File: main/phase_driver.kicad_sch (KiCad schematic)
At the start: 12 parts, among them Q201 TK4R3E06PL, Q202 TK4R3E06PL, U201 LM2105

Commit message: Start route PCB
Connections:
- net INH: now also U201.2 (INH); no longer U201. (VDD)
- net INL: now also U201.3 (INL); no longer U201. (VDD)
- net OUT: now also U201.6 (SH); no longer U201. (VDD)
- net V_{DRIVE}: now also U201.1 (VDD); no longer U201. (VDD)
- net at C202.1: now also U201.8 (BST); no longer U201. (VDD)
- net at Q202.1 (G): now also U201.5 (GL); no longer U201. (VDD)
- net at Q201.1 (G): now also U201.7 (GH); no longer U201. (VDD)
- net PGND renamed GND
- net GND: now also U201.4 (GND), U201.9 (GND); no longer U201. (VDD)
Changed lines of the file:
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@@
 			)
 		)
-		(pin ""
+		(pin "3"
 		)
-		(pin ""
+		(pin "9"
 		)
-		(pin ""
+		(pin "6"
 		)
-		(pin ""
+		(pin "1"
 		)
-		(pin ""
+		(pin "4"
 		)
-		(pin ""
+		(pin "7"
 		)
-		(pin ""
+		(pin "2"
 		)
-		(pin ""
+		(pin "5"
+		)
+		(pin "8"
 		)
 		(instances

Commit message: Route of power rails
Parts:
- removed C201, C204: 1n, Capacitor_SMD:C_0805_2012Metric, symbol Device:C

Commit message: Clean silkscreen
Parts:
- renumbered C202 to C1001, C203 to C1002, C205 to C1003, D201 to D1001, D202 to D1002, Q201 to Q1001, Q202 to Q1002, R201 to R1001, R202 to R1002, U201 to U1001

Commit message: Sent to fab
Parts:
- C1001: MPN (none) -> CL21B104KACNFNC; Mouser SKU (none) -> 187-CL21B104KACNFNC
- C1003: MPN (none) -> CL21B105KLFVPNE; Mouser SKU (none) -> 187-CL21B105KLFVPNE
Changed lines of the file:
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@@
+			)
+		)
+		(property "Quantity" ""
+			(at 190.5 57.15 0)
+			(effects
+				(font
+					(size 1.27 1.27)
+				)
 			)
 		)
@@
 			)
 		)
+		(property "MPN" "CL21B104KACNFNC "
+			(at 140.97 58.42 0)
+			(effects
+				(font
+					(size 1.27 1.27)
+				)
+			)
+		)
+		(property "Mouser SKU" " 187-CL21B104KACNFNC "
+			(at 140.97 58.42 0)
+			(effects
+				(font
+					(size 1.27 1.27)
+				)
+			)
+		)
+		(property "Quantity" ""
+			(at 140.97 58.42 0)
+			(effects
+				(font
+					(size 1.27 1.27)
+				)
+			)
+		)
 		(pin "1"
 		)
@@
 			)
 		)
+		(property "Quantity" ""
+			(at 228.6 68.58 0)
+			(effects
+				(font
+					(size 1.27 1.27)
+				)
+			)
+		)
 		(pin "1"
 		)
@@
 			)
 		)
+		(property "Quantity" ""
+			(at 83.82 87.63 0)
+			(effects
+				(font
+					(size 1.27 1.27)
+				)
+			)
+		)
 		(pin "1"
 		)
@@
 			)
 		)
+		(property "Quantity" ""
+			(at 121.92 66.04 0)
+			(effects
+				(font
+					(size 1.27 1.27)
+				)
+			)
+		)
 		(pin "3"
 		)
@@
 			)
 		)
+		(property "Quantity" ""
+			(at 168.91 78.74 0)
+			(effects
+				(font
+					(size 1.27 1.27)
+				)
+			)
+		)
 		(pin "1"
 		)
@@
 			)
 		)
+		(property "Quantity" ""
+			(at 93.98 87.63 0)
+			(effects
+				(font
+					(size 1.27 1.27)
+				)
+			)
+		)
 		(pin "1"
 		)
@@
 			)
 		)
+		(property "Quantity" ""
+			(at 190.5 78.74 0)
+			(effects
+				(font
+					(size 1.27 1.27)
+				)
+			)
+		)
 		(pin "2"
 		)
@@
 			)
 		)
+		(property "Quantity" ""
+			(at 168.91 57.15 0)
+			(effects
+				(font
+					(size 1.27 1.27)
+				)
+			)
+		)
 		(pin "1"
 		)
@@
 			)
 		)
+		(property "MPN" "CL21B105KLFVPNE "
+			(at 109.22 87.63 0)
+			(effects
+				(font
+					(size 1.27 1.27)
+				)
+			)
+		)
+		(property "Mouser SKU" " 187-CL21B105KLFVPNE "
+			(at 109.22 87.63 0)
+			(effects
+				(font
+					(size 1.27 1.27)
+				)
+			)
+		)
+		(property "Quantity" ""
+			(at 109.22 87.63 0)
+			(effects
+				(font
+					(size 1.27 1.27)
+				)
+			)
+		)

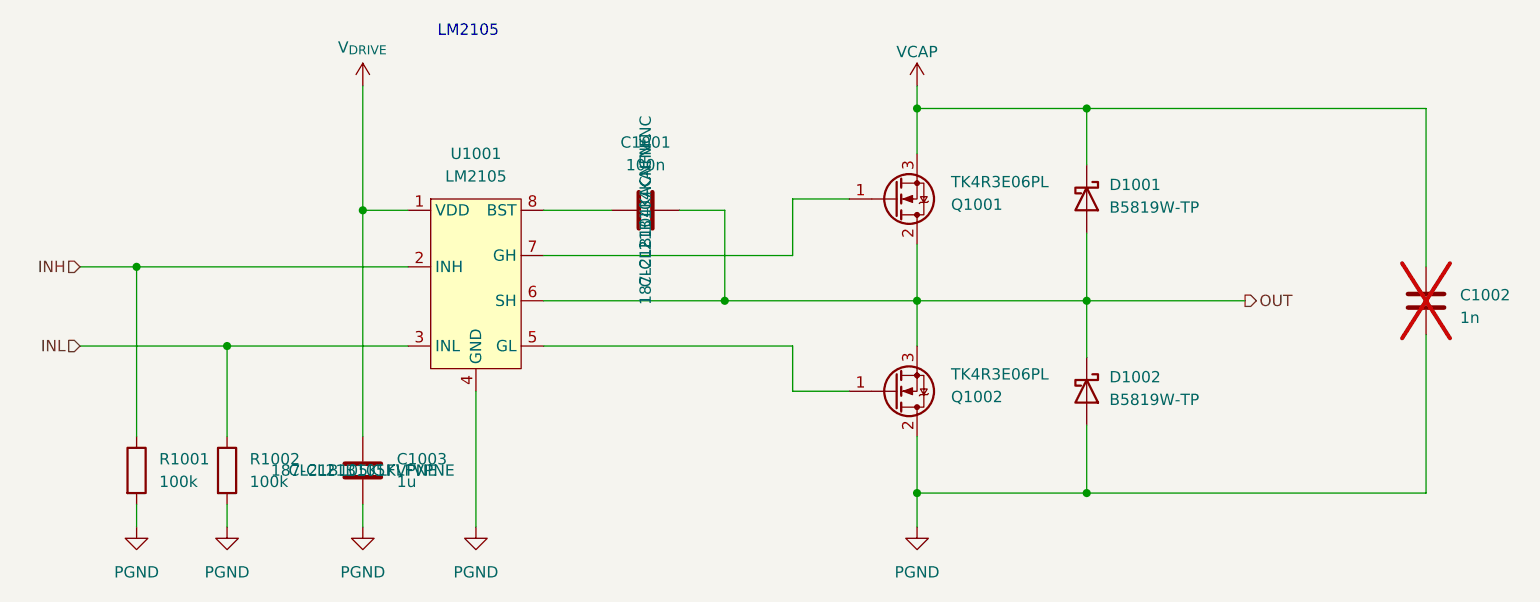
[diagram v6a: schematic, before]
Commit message: BOM almost OK, starts new side board.
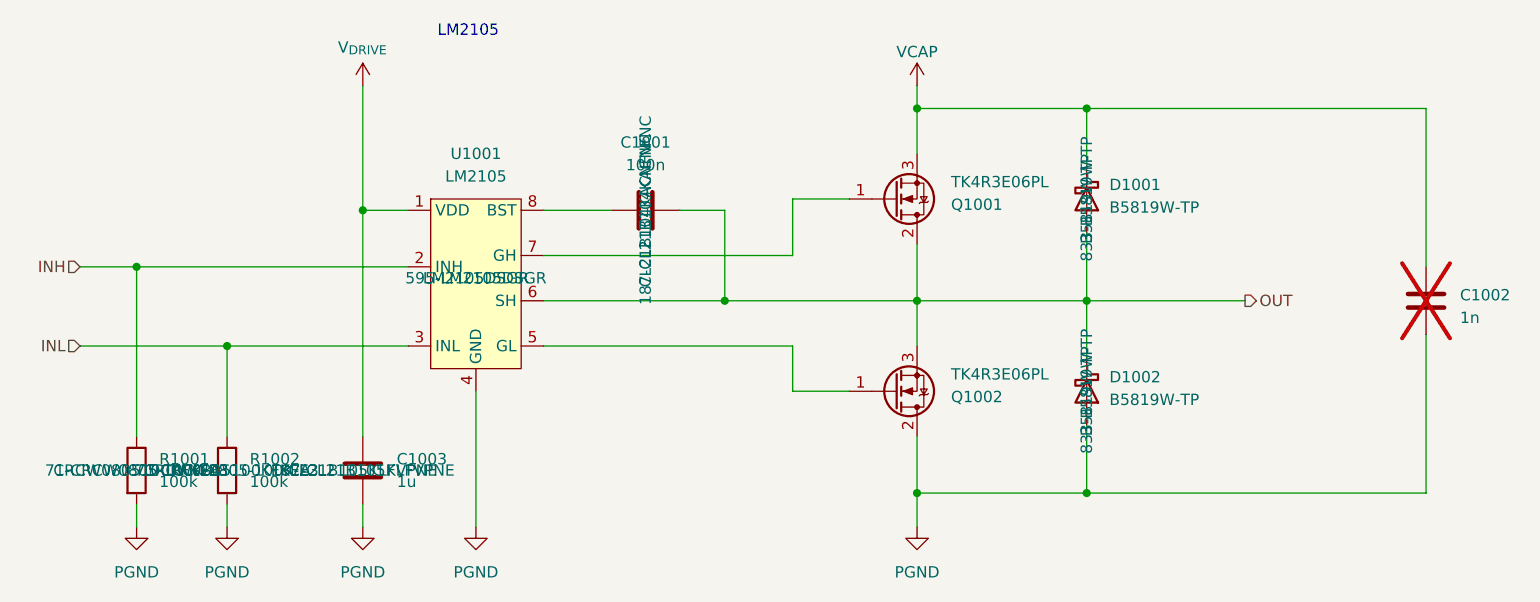
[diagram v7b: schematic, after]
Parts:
- D1001, D1002: MPN (none) -> B5819W-TP; Mouser SKU (none) -> 833-B5819W-TP
- R1001, R1002: MPN (none) -> CRCW0805100KFKEA; Mouser SKU (none) -> 71-CRCW0805-100K-E3
- U1001: MPN (none) -> LM2105DSGR; Mouser SKU (none) -> 595-LM2105DSGR
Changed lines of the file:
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@@
 (kicad_sch
-	(version 20240101)
+	(version 20240417)
 	(generator "eeschema")
 	(generator_version "8.99")
@@
 			)
 		)
+		(property "MPN" " B5819W-TP "
+			(at 190.5 57.15 0)
+			(effects
+				(font
+					(size 1.27 1.27)
+				)
+			)
+		)
+		(property "Mouser SKU" " 833-B5819W-TP "
+			(at 190.5 57.15 0)
+			(effects
+				(font
+					(size 1.27 1.27)
+				)
+			)
+		)
 		(pin "2"
 		)
@@
 			)
 		)
+		(property "MPN" "CRCW0805100KFKEA"
+			(at 83.82 87.63 0)
+			(effects
+				(font
+					(size 1.27 1.27)
+				)
+			)
+		)
+		(property "Mouser SKU" " 71-CRCW0805-100K-E3 "
+			(at 83.82 87.63 0)
+			(effects
+				(font
+					(size 1.27 1.27)
+				)
+			)
+		)
 		(pin "1"
 		)
@@
 			)
 		)
-		(property "MPN" ""
+		(property "MPN" " LM2105DSGR "
 			(at 121.92 66.04 0)
 			(effects
@@
 		)
 		(property "Quantity" ""
+			(at 121.92 66.04 0)
+			(effects
+				(font
+					(size 1.27 1.27)
+				)
+			)
+		)
+		(property "Mouser SKU" " 595-LM2105DSGR "
 			(at 121.92 66.04 0)
 			(effects
@@
 			)
 		)
+		(property "MPN" "CRCW0805100KFKEA"
+			(at 93.98 87.63 0)
+			(effects
+				(font
+					(size 1.27 1.27)
+				)
+			)
+		)
+		(property "Mouser SKU" " 71-CRCW0805-100K-E3 "
+			(at 93.98 87.63 0)
+			(effects
+				(font
+					(size 1.27 1.27)
+				)
+			)
+		)
 		(pin "1"
 		)
@@
 			(at 190.5 78.74 0)
 			(effects
+				(font
+					(size 1.27 1.27)
+				)
+			)
+		)
+		(property "MPN" " B5819W-TP "
+			(at 190.5 78.74 0)
+			(effects
+				(font
+					(size 1.27 1.27)
+				)
+			)
+		)
+		(property "Mouser SKU" " 833-B5819W-TP "
+			(at 190.5 78.74 0)
+			(effects

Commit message: Revised with BOM ordered
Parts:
- C1001: Mouser SKU 187-CL21B104KACNFNC -> 187-CL21B104KACNFNC
- C1003: Mouser SKU 187-CL21B105KLFVPNE -> 187-CL21B105KLFVPNE
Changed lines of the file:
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@@
 			)
 		)
-		(property "Mouser SKU" " 187-CL21B104KACNFNC "
+		(property "Mouser SKU" "187-CL21B104KACNFNC "
 			(at 140.97 58.42 0)
 			(effects
@@
 			)
 		)
-		(property "Mouser SKU" " 187-CL21B105KLFVPNE "
+		(property "Mouser SKU" "187-CL21B105KLFVPNE "
 			(at 109.22 87.63 0)
 			(effects
